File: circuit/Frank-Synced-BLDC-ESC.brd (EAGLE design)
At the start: 48.3 x 25.4 mm, 57 parts, among them IC1 Vreg +5V, Q1 PMOS-DPAK, Q2 NMOS-DPAK, Q4 PMOS-DPAK, Q5 NMOS-DPAK, Q7 PMOS-DPAK, Q8 NMOS-DPAK, U1 ATMEGA168MLF, U2 OSC-16MHz

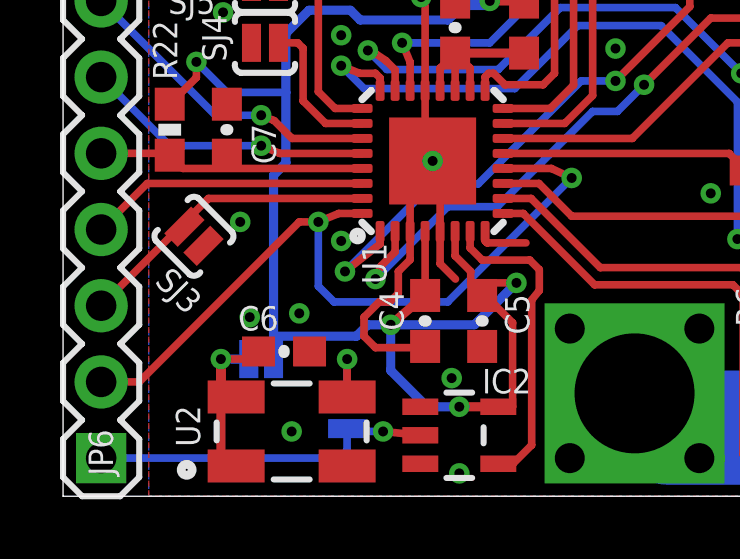
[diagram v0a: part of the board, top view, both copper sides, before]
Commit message: layout for 7 x 5 mm 5V oscillator
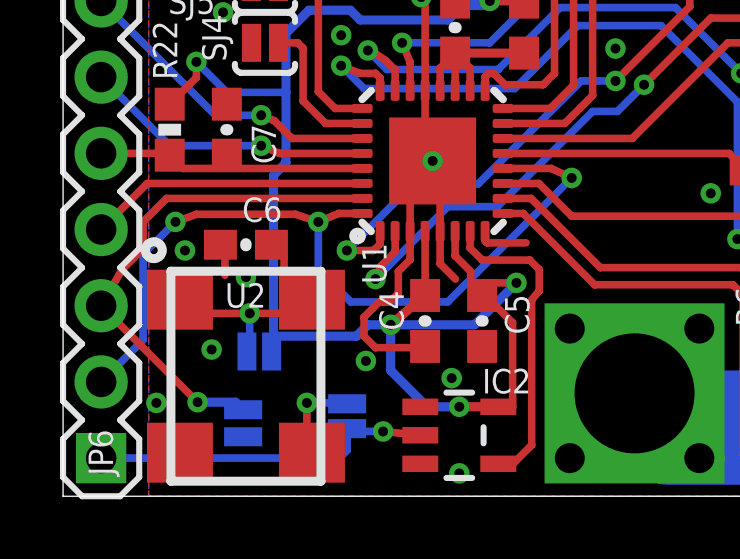
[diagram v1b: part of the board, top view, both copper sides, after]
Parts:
- U2: device Frank-Synced-BLDC-ESC:CRYSTAL-OSC-SMD-5X3 -> Frank-Synced-BLDC-ESC:OSCILLATOR-7X5
- moved SJ3 6.45 mm to (6.00, 2.43), flipped to the bottom, turned to 90 degrees
- moved C6 3.78 mm to (6.10, 8.38), turned to 180 degrees
- moved U2 2.39 mm to (6.10, 4.00), turned to 270 degrees
- moved SJ2 0.26 mm to (6.54, 4.83)
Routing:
- net TXD: track 10.2 -> 17.1 mm, vias 0 -> 1
- net PWM: track 25.8 -> 27.3 mm, vias 2 -> 3
- net N$25: track 8.13 -> 9.10 mm
- net GATE_N-C: track 32.8 -> 32.2 mm
- net GND: track 44.4 -> 45.0 mm
